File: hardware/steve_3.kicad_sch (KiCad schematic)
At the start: 18 parts, among them Q2 Q_NMOS_GSD, Q3 Q_NMOS_GSD, Q4 Q_NMOS_GSD, Q5 Q_NMOS_GSD, Q6 Q_NMOS_GSD

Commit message: Schematic and Board fixes for Mfg
Schematic and Board fixes for Manufacturing. Added LCSC/JLC part numbers to values in schematic for BOM processing. Updated schematic fields. Added GND to each PSM connector. Brought PSM connector fix to PCB. Updated PCB designator locations from schematic changes.
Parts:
- ADC1, SPI2, UART1: value TerminalBlock_1770979_4pos_Vertical -> 5A Spring Conn 4pos C3818616
- J1: renamed from PSM-1; value PSM-Servo -> JST GH 6P Vertical 1A C189892
- J2: renamed from PSM-2; value PSM-MOSFET_BATT1 -> JST GH 6P Vertical 1A C189892
- J3: renamed from PSM-3; value PSM_Cont -> JST GH 6P Vertical 1A C189892
- Q2, Q3, Q4, Q5, Q6: value Q_NMOS_GSD -> NMOS GSD 350mA 60V C282405
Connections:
- net BATT1_V: now also J1.5 (Pin_5); no longer J2.6 (Pin_6)
- net CONT4_V_BATT: now also J3.5 (Pin_5); no longer J3.4 (Pin_4)
- net CONT5_V_BATT: now also J3.6 (Pin_6); no longer J3.5 (Pin_5)
- net GND: now also J1.4 (Pin_4), J2.4 (Pin_4), J3.4 (Pin_4)
- net MOSFET_4: now also J2.5 (Pin_5); no longer J2.4 (Pin_4)
- net MOSFET_5: now also J2.6 (Pin_6); no longer J2.5 (Pin_5)
- net SERVO_PWM_4: now also J1.6 (Pin_6); no longer J1.4 (Pin_4)
- no-connect marks 3 -> 0
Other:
- moved on the sheet: J1, J2, J3

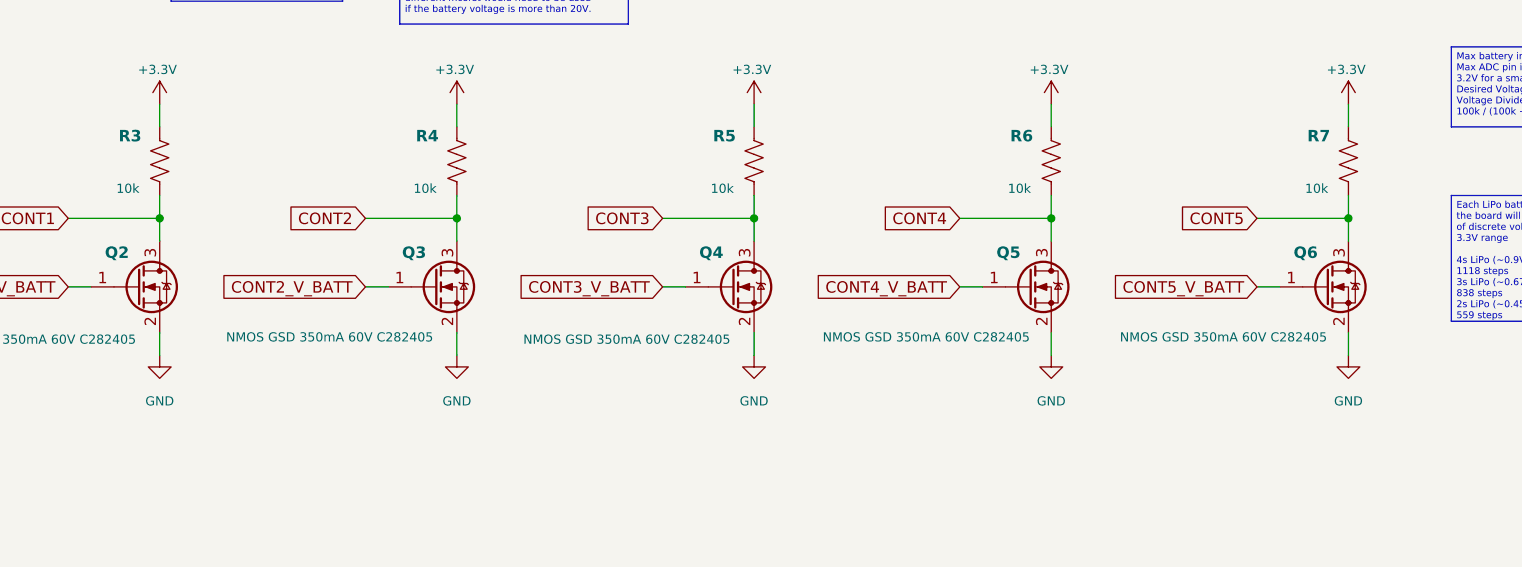
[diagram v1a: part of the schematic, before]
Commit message: Fixed all ERC issues; fixed important DRC issues
Fixed all ERC Errors and Warnings in the schematic. Fixed all Errors and Warnings in the DRC for the board (Not counting JLC 4-Wire Kelvin test and plane thermal relief spoke errors that were manually reviewed and excluded).
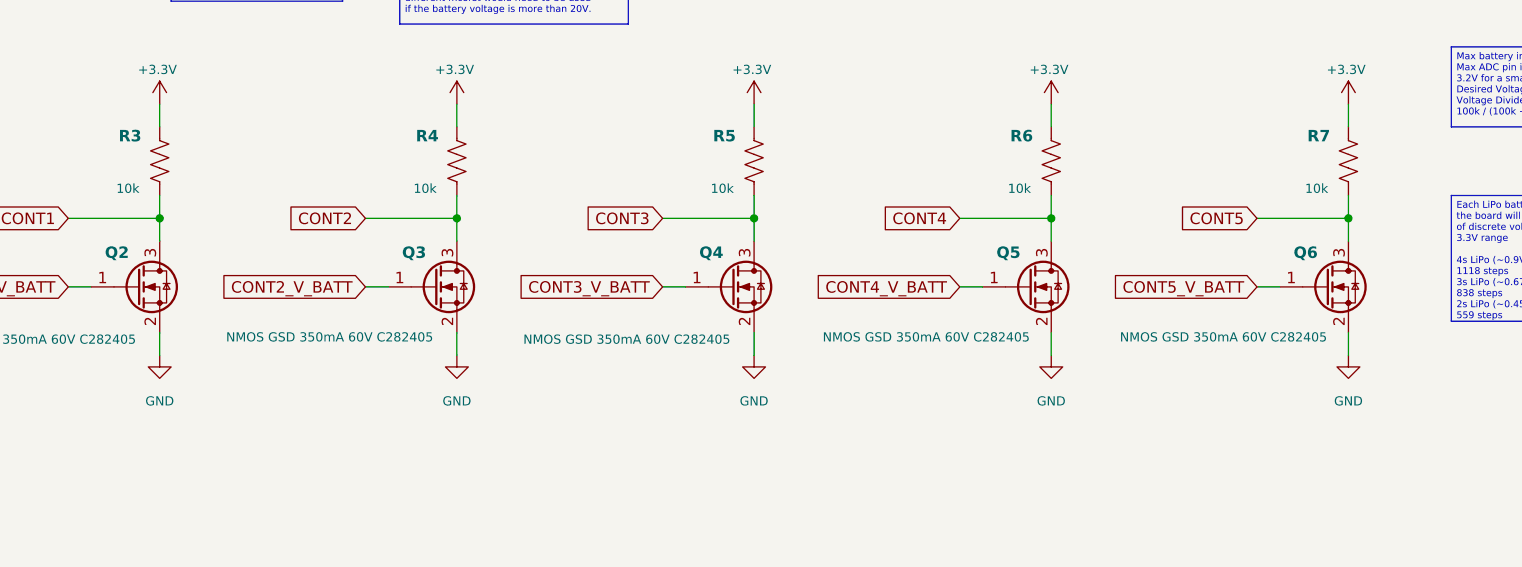
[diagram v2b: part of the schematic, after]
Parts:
- Q2, Q3, Q4, Q5, Q6: symbol Device:Q_NMOS_GSD -> Transistor_FET:Q_NMOS_GSD
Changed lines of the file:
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@@
 	)
 	(symbol
+		(lib_name "TerminalBlock_1770979_4pos_Vertical_2")
 		(lib_id "Imported_Symbols:TerminalBlock_1770979_4pos_Vertical")
 		(at 115.57 114.3 0)
@@
 	)
 	(symbol
-		(lib_id "Device:Q_NMOS_GSD")
+		(lib_id "Transistor_FET:Q_NMOS_GSD")
 		(at 87.63 52.07 0)
 		(unit 1)
@@
 	)
 	(symbol
-		(lib_id "Device:Q_NMOS_GSD")
+		(lib_id "Transistor_FET:Q_NMOS_GSD")
 		(at 186.69 52.07 0)
 		(unit 1)
@@
 	)
 	(symbol
-		(lib_id "Device:Q_NMOS_GSD")
+		(lib_id "Transistor_FET:Q_NMOS_GSD")
 		(at 219.71 52.07 0)
 		(unit 1)
@@
 	)
 	(symbol
-		(lib_id "Device:Q_NMOS_GSD")
+		(lib_id "Transistor_FET:Q_NMOS_GSD")
 		(at 153.67 52.07 0)
 		(unit 1)
@@
 	)
 	(symbol
-		(lib_id "Device:Q_NMOS_GSD")
+		(lib_id "Transistor_FET:Q_NMOS_GSD")
 		(at 120.65 52.07 0)
 		(unit 1)
@@
 	)
 	(symbol
+		(lib_name "TerminalBlock_1770979_4pos_Vertical_1")
 		(lib_id "Imported_Symbols:TerminalBlock_1770979_4pos_Vertical")
 		(at 46.99 114.3 0)
